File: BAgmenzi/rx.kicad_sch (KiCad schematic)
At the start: 37 parts, among them IC1 TPL0501-100RSER, U2 AD8338ACPZ-R7, U3 OPA836IDBVT, U4 OPA836IDBVT, U5 TPS22916CYFPR, U6 TPS22916CYFPR

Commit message: added libraries, other changes in sch, started pcb
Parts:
- removed C31, C32: 2.2u, symbol Device:C
- removed R14: 10k, symbol Device:R
- removed TP4: vga_pwr_en, symbol Connector:TestPoint
- removed TP5: preamp_pwr_en, symbol Connector:TestPoint
- removed U5: TPS22916CYFPR, BGA4C40P2X2_78X78X50:BGA4C40P2X2_78X78X50, symbol TPS22916CYFPR:TPS22916CYFPR
- removed U6: TPS22916CYFPR, BGA4C40P2X2_78X78X50, symbol TPS22916CYFPR:TPS22916CYFPR
- C19, C20, C21, C22, C23, C24, C25, C26, C27, C29, C30: footprint (none) -> Capacitor_SMD:C_0402_1005Metric
- C28: footprint Capacitor_SMD:C_0201_0603Metric -> Capacitor_SMD:C_0402_1005Metric
- C31: renamed from C63; footprint (none) -> Capacitor_SMD:C_0402_1005Metric
- C34: renamed from C33; footprint (none) -> Capacitor_SMD:C_0402_1005Metric
- IC1: footprint RSE0008A -> KiCad:RSE0008A
- R10, R11, R12, R13, R15, R16, R7, R8, R9: footprint (none) -> Resistor_SMD:R_0402_1005Metric
- TP2: footprint (none) -> TestPoint:TestPoint_Loop_D2.50mm_Drill1.85mm
- TP6: footprint (none) -> TestPoint:TestPoint_Loop_D2.50mm_Drill1.0mm_LowProfile
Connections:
- net +V_PREAMP is gone; now on net V_RX: C23.2, C24.2, U3.6 (VS+)
- net +V_VGA is gone; now on net V_RX: C19.2, C20.2, U2.15 (VBAT), U2.6 (MODE)
- net PREAMP_PWR_EN renamed VRX_EN
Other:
- moved on the sheet: C34, IC1, R15, R16, TP6

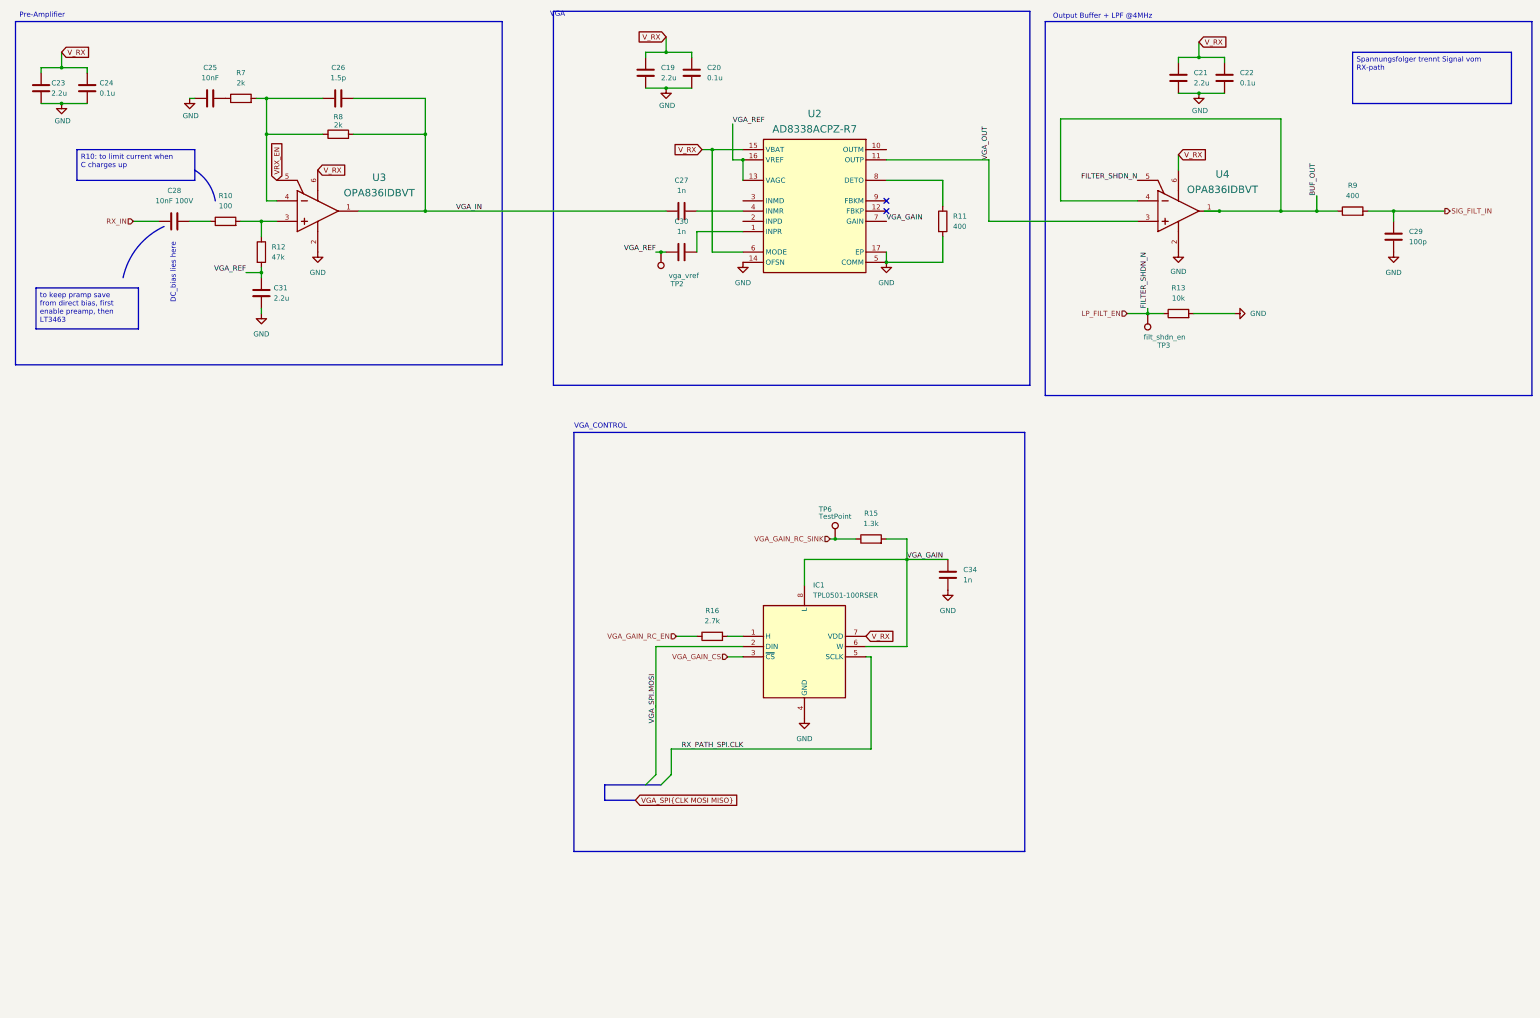
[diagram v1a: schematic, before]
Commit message: changed VRX rail and deleted U12
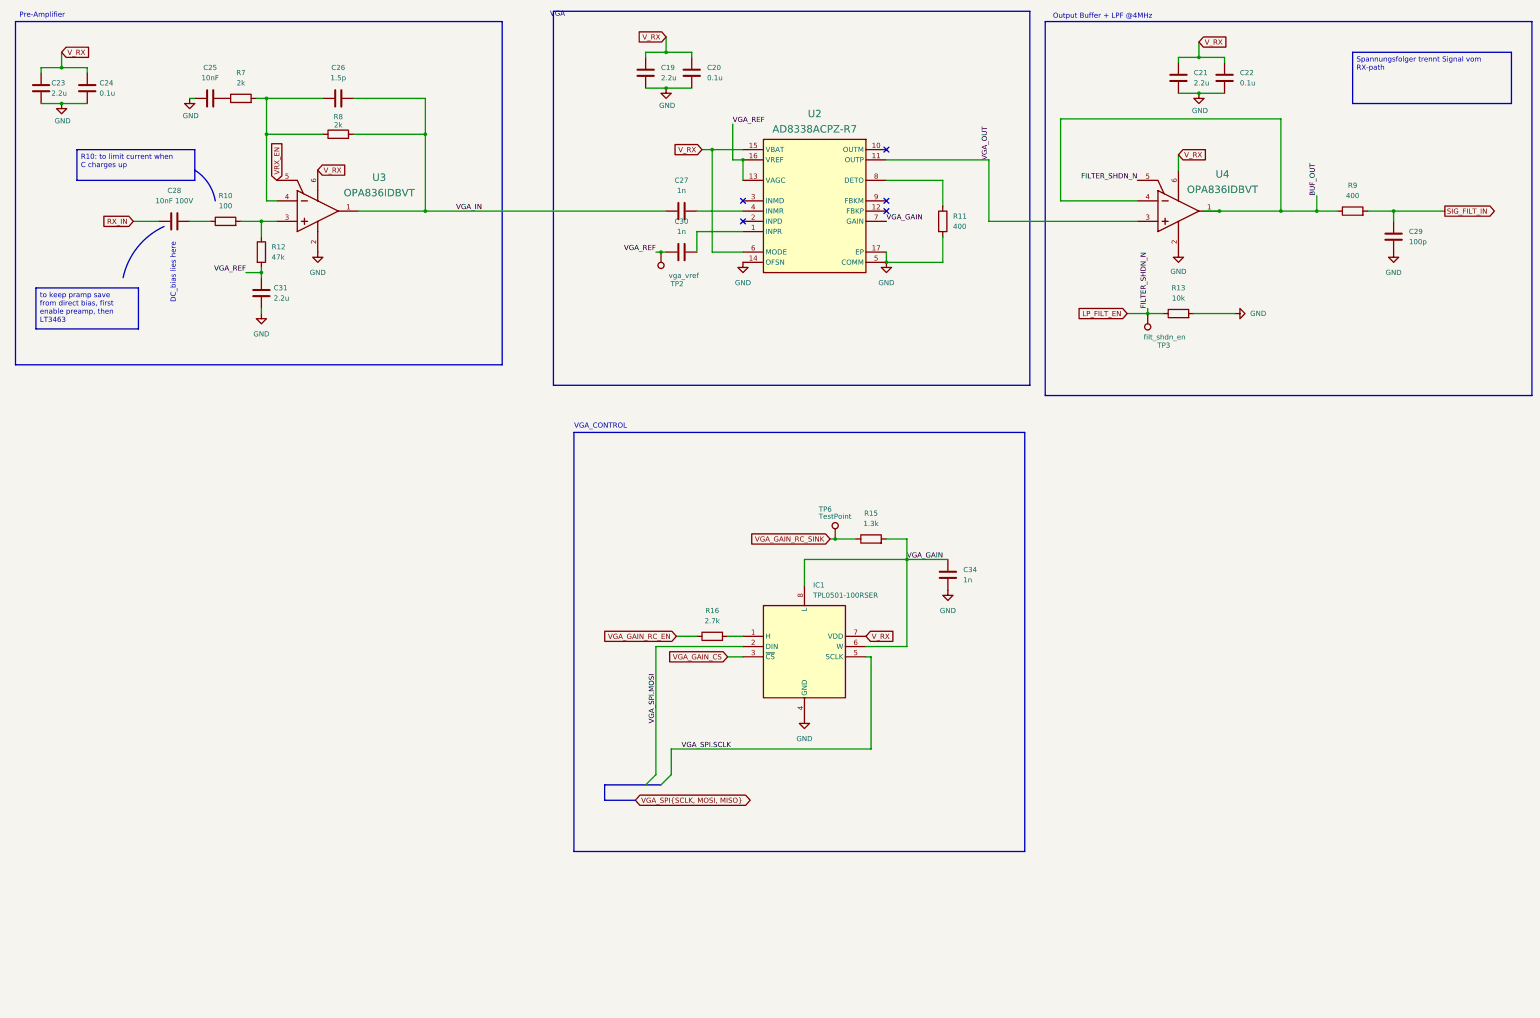
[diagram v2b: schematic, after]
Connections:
- net RX_PATH_SPI.CLK renamed VGA_SPI.SCLK
- no-connect marks 2 -> 5
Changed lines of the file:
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@@
+	)
+	(no_connect
+		(at 234.95 54.61)
+	)
+	(no_connect
+		(at 199.39 72.39)
+	)
+	(no_connect
+		(at 199.39 67.31)
 	)
 	(no_connect
@@
 		)
 	)
-	(label "RX_PATH_SPI.CLK"
+	(label "VGA_SPI.SCLK"
 		(at 184.15 203.2 0)
 		(effects
@@
 		)
 	)
-	(global_label "VGA_SPI{CLK MOSI MISO}"
-		(shape input)
+	(global_label "VGA_SPI{SCLK, MOSI, MISO}"
+		(shape bidirectional)
 		(at 172.72 215.9 0)
 		(fields_autoplaced yes)
@@
 		)
 		(property "Intersheetrefs" "${INTERSHEET_REFS}"
-			(at 199.5934 215.9 0)
+			(at 203.1238 215.9 0)
 			(effects
 				(font
@@
 		)
 	)
+	(global_label "VGA_GAIN_CS"
+		(shape input)
+		(at 195.58 180.34 180)
+		(fields_autoplaced yes)
+		(effects
+			(font
+				(size 1.27 1.27)
+			)
+			(justify right)
+		)
+		(property "Intersheetrefs" "${INTERSHEET_REFS}"
+			(at 180.439 180.34 0)
+			(effects
+				(font
+					(size 1.27 1.27)
+				)
+				(justify right)
+			)
+		)
+	)
+	(global_label "SIG_FILT_IN"
+		(shape output)
+		(at 373.38 69.85 0)
+		(fields_autoplaced yes)
+		(effects
+			(font
+				(size 1.27 1.27)
+			)
+			(justify left)
+		)
+		(property "Intersheetrefs" "${INTERSHEET_REFS}"
+			(at 387.0091 69.85 0)
+			(effects
+				(font
+					(size 1.27 1.27)
+				)
+				(justify left)
+			)
+		)
+	)
 	(global_label "V_RX"
 		(shape input)
@@
 		)
 	)
+	(global_label "LP_FILT_EN"
+		(shape input)
+		(at 294.64 95.25 180)
+		(fields_autoplaced yes)
+		(effects
+			(font
+				(size 1.27 1.27)
+			)
+			(justify right)
+		)
+		(property "Intersheetrefs" "${INTERSHEET_REFS}"
+			(at 281.2529 95.25 0)
+			(effects
+				(font
+					(size 1.27 1.27)
+				)
+				(justify right)
+			)
+		)
+	)
+	(global_label "RX_IN"
+		(shape input)
+		(at 48.26 72.39 180)
+		(fields_autoplaced yes)
+		(effects
+			(font
+				(size 1.27 1.27)
+			)
+			(justify right)
+		)
+		(property "Intersheetrefs" "${INTERSHEET_REFS}"
+			(at 39.8924 72.39 0)
+			(effects
+				(font
+					(size 1.27 1.27)
+				)
+				(justify right)
+			)
+		)
+	)
 	(global_label "V_RX"
 		(shape input)
@@
 		)
 	)
+	(global_label "VGA_GAIN_RC_EN"
+		(shape input)
+		(at 182.88 175.26 180)
+		(fields_autoplaced yes)
+		(effects
+			(font
+				(size 1.27 1.27)
+			)
+			(justify right)
+		)
+		(property "Intersheetrefs" "${INTERSHEET_REFS}"
+			(at 164.2314 175.26 0)
+			(effects
+				(font
+					(size 1.27 1.27)
+				)
+				(justify right)
+			)
+		)
+	)
 	(global_label "VRX_EN"
 		(shape input)
@@
 		)
 	)
+	(global_label "VGA_GAIN_RC_SINK"
+		(shape input)
+		(at 220.98 151.13 180)
+		(fields_autoplaced yes)
+		(effects
+			(font
+				(size 1.27 1.27)
+			)
+			(justify right)
+		)
+		(property "Intersheetrefs" "${INTERSHEET_REFS}"
+			(at 200.3961 151.13 0)
+			(effects
+				(font
+					(size 1.27 1.27)
+				)
+				(justify right)
+			)
+		)
+	)
 	(global_label "V_RX"
 		(shape input)
@@
 		)
 	)
-	(hierarchical_label "VGA_GAIN_CS"
-		(shape input)
-		(at 195.58 180.34 180)
-		(effects
-			(font
-				(size 1.27 1.27)
-			)
-			(justify right)
-		)
-	)
-	(hierarchical_label "RX_IN"
-		(shape input)
-		(at 48.26 72.39 180)
-		(effects
-			(font
-				(size 1.27 1.27)
-			)
-			(justify right)
-		)
-	)
-	(hierarchical_label "VGA_GAIN_RC_EN"
-		(shape input)
-		(at 182.88 175.26 180)
-		(effects
-			(font
-				(size 1.27 1.27)
-			)
-			(justify right)
-		)
-	)
-	(hierarchical_label "VGA_GAIN_RC_SINK"
-		(shape input)
-		(at 220.98 151.13 180)
-		(effects
-			(font
-				(size 1.27 1.27)
-			)
-			(justify right)
-		)
-	)
-	(hierarchical_label "SIG_FILT_IN"
-		(shape output)
-		(at 373.38 69.85 0)
-		(effects
-			(font
-				(size 1.27 1.27)
-			)
-			(justify left)
-		)
-	)
-	(hierarchical_label "LP_FILT_EN"
-		(shape input)
-		(at 294.64 95.25 180)
-		(effects
-			(font
-				(size 1.27 1.27)
-			)
-			(justify right)
-		)
-	)

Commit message: started layout, front v backside
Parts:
- TP2: footprint TestPoint:TestPoint_Loop_D2.50mm_Drill1.85mm -> TestPoint:TestPoint_Pad_D2.0mm
- TP6: footprint TestPoint:TestPoint_Loop_D2.50mm_Drill1.0mm_LowProfile -> TestPoint:TestPoint_Pad_D2.0mm
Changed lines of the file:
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@@
 	)
 	(rectangle
-		(start 19.05 22.86)
-		(end 139.7 107.95)
+		(start 19.05 21.59)
+		(end 139.7 106.68)
 		(stroke
 			(width 0)
@@
 	)
 	(junction
+		(at 120.65 69.85)
+		(diameter 0)
+		(color 0 0 0 0)
+	)
+	(junction
 		(at 80.01 85.09)
 		(diameter 0)
@@
 	)
 	(junction
-		(at 120.65 69.85)
-		(diameter 0)
-		(color 0 0 0 0)
-	)
-	(junction
 		(at 191.77 54.61)
 		(diameter 0)
@@
 			)
 		)
-		(property "Footprint" "TestPoint:TestPoint_Loop_D2.50mm_Drill1.85mm"
+		(property "Footprint" "TestPoint:TestPoint_Pad_D2.0mm"
 			(at 173.99 80.01 0)
 			(effects
@@
 			)
 		)
-		(property "Footprint" "TestPoint:TestPoint_Loop_D2.50mm_Drill1.0mm_LowProfile"
+		(property "Footprint" "TestPoint:TestPoint_Pad_D2.0mm"
 			(at 227.33 151.13 0)
 			(effects

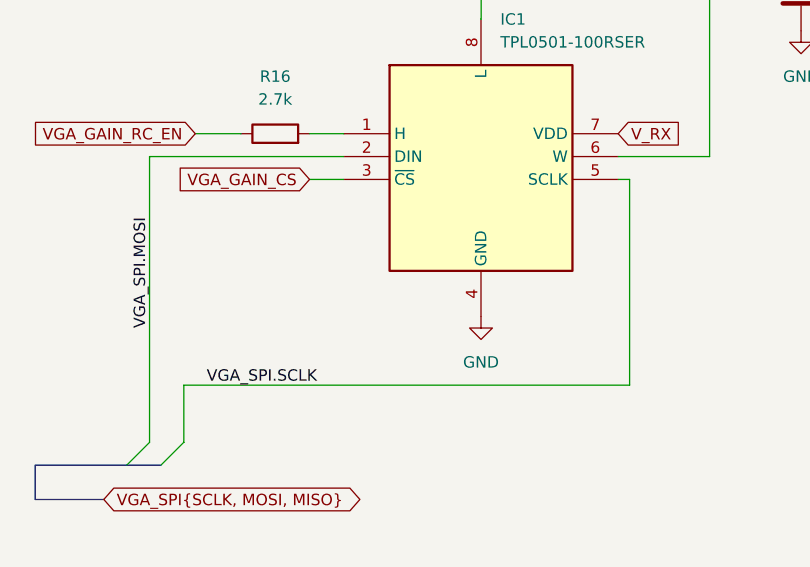
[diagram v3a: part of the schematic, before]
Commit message: started routing, changed enable signals to nRF
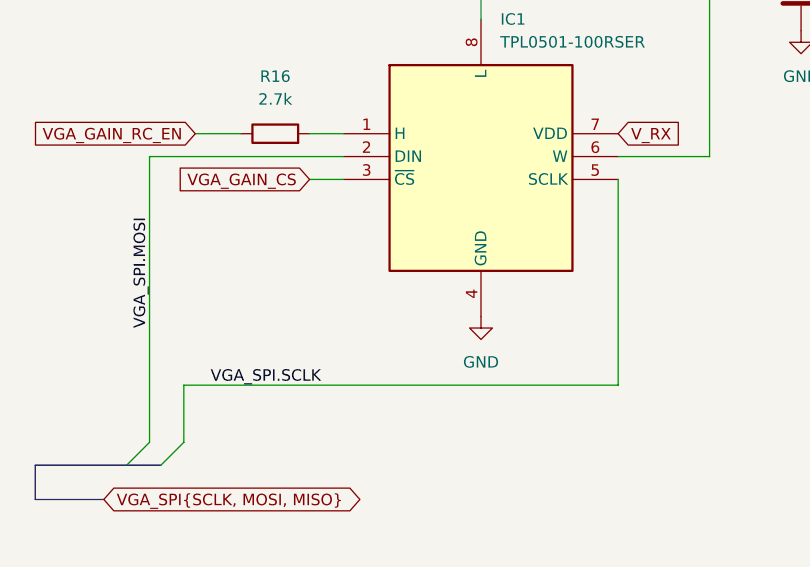
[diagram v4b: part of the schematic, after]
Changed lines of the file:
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@@
+	(wire
+		(pts
+			(xy 229.87 203.2) (xy 229.87 180.34)
+		)
+		(stroke
+			(width 0)
+			(type default)
+		)
+	)
 	(wire
 		(pts
@@
 	(wire
 		(pts
-			(xy 181.61 203.2) (xy 231.14 203.2)
-		)
-		(stroke
-			(width 0)
-			(type default)
-		)
-	)
-	(wire
-		(pts
-			(xy 231.14 180.34) (xy 231.14 203.2)
+			(xy 181.61 203.2) (xy 229.87 203.2)
 		)
 		(stroke
@@
 		(pts
 			(xy 187.96 74.93) (xy 199.39 74.93)
-		)
-		(stroke
-			(width 0)
-			(type default)
-		)
-	)
-	(wire
-		(pts
-			(xy 231.14 180.34) (xy 229.87 180.34)
 		)
 		(stroke
@@
 	)
 	(label "VGA_SPI.SCLK"
-		(at 184.15 203.2 0)
-		(effects
-			(font
-				(size 1.27 1.27)
-			)
-			(justify left bottom)
+		(at 196.85 203.2 180)
+		(effects
+			(font
+				(size 1.27 1.27)
+			)
+			(justify right bottom)
 		)
 	)
@@
 		(shape input)
 		(at 182.88 175.26 180)
-		(fields_autoplaced yes)
-		(effects
-			(font
+		(effects
+			(font

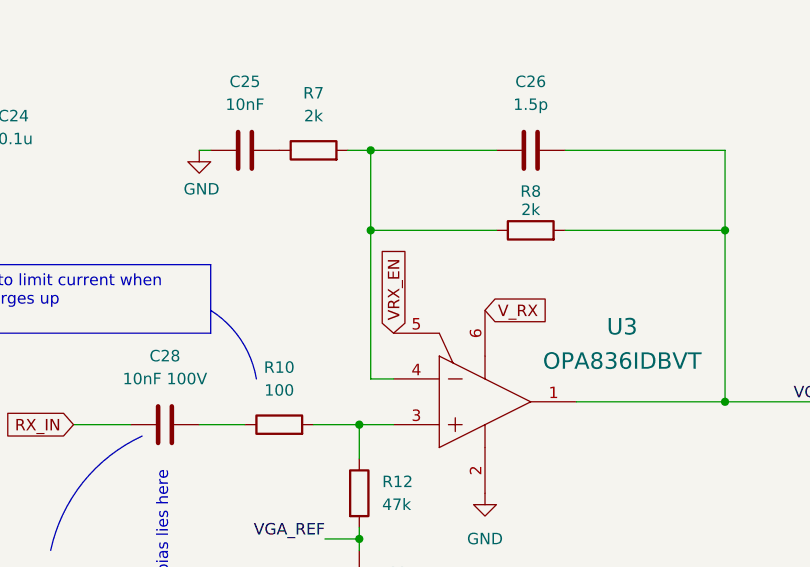
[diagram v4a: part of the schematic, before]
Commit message: routed msp and nrf
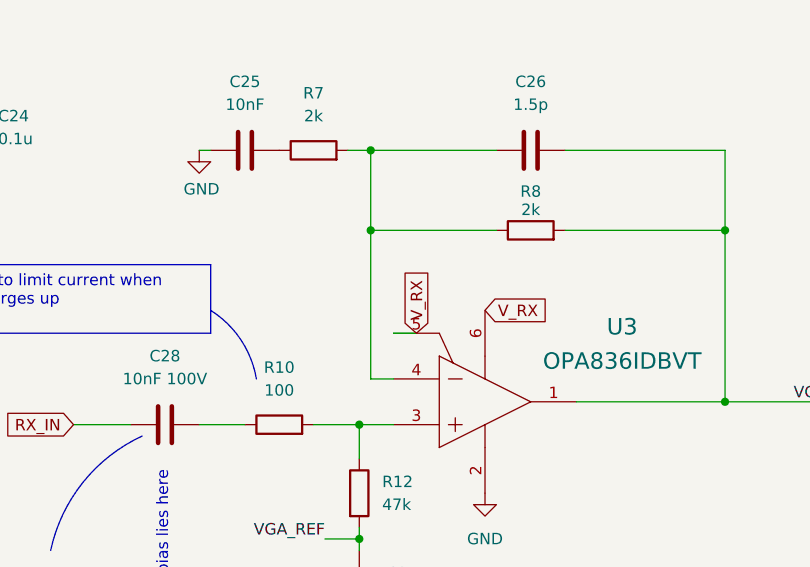
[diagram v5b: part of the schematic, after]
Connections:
- net VRX_EN is gone; now on net V_RX: U3.5 (~{PD})
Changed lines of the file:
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@@
+	(wire
+		(pts
+			(xy 86.36 62.23) (xy 83.82 62.23)
+		)
+		(stroke
+			(width 0)
+			(type default)
+		)
+	)
 	(wire
 		(pts
@@
 		)
 	)
+	(global_label "V_RX"
+		(shape input)
+		(at 86.36 62.23 90)
+		(fields_autoplaced yes)
+		(effects
+			(font
+				(size 1.27 1.27)
+			)
+			(justify left)
+		)
+		(property "Intersheetrefs" "${INTERSHEET_REFS}"
+			(at 86.36 54.7091 90)
+			(effects
+				(font
+					(size 1.27 1.27)
+				)
+				(justify left)
+			)
+		)
+	)
 	(global_label "SIG_FILT_IN"
 		(shape output)
@@
 			)
 		)
-	)
-	(global_label "VRX_EN"
-		(shape input)
-		(at 83.82 62.23 90)
-		(fields_autoplaced yes)
-		(effects
-			(font
-				(size 1.27 1.27)
-			)
-			(justify left)
-		)
-		(property "Intersheetrefs" "${INTERSHEET_REFS}"
-			(at 83.82 52.2296 90)
-			(effects
-				(font
-					(size 1.27 1.27)
-				)
-				(justify left)
-			)
-		)

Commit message: powerplanes
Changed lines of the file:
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@@
 		(on_board yes)
 		(dnp no)
-		(fields_autoplaced yes)
 		(property "Reference" "C30"
-			(at 184.15 72.39 90)
+			(at 184.15 74.168 90)
 			(effects
 				(font
@@
 		)
 		(property "Value" "1n"
-			(at 184.15 74.93 90)
+			(at 183.896 76.454 90)
 			(effects
 				(font
